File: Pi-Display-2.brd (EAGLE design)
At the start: 24.8 x 64.8 mm, 13 parts, among them IC1 MCP2515-I/SO, IC2 MCP2562-E/SN, J1 RJ45 CAN.Bus, Q1 16MHz, U1 TSR 2-2450

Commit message: Layouts angepasst
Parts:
- added C7: 10µF/25V, rcl:C1206
- C6: value 22µF 50V Low-ESR -> 10µF/25V; device rcl:E2-5 -> rcl:C1206
- moved C6 2.17 mm to (21.0, 58.1), flipped to the bottom, turned to 270 degrees
- moved C2 1.62 mm to (22.2, 31.8)
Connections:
- net +24V: now also C6.1, C7.1; no longer C6.+
- net GND: now also C6.2, C7.2; no longer C6.-
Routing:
- net GND: track 9.68 -> 12.4 mm
- net +5V: track 95.2 -> 96.9 mm
- net SPI_MOSI: track 7.75 -> 9.02 mm
- net +24V: track 64.4 -> 65.0 mm

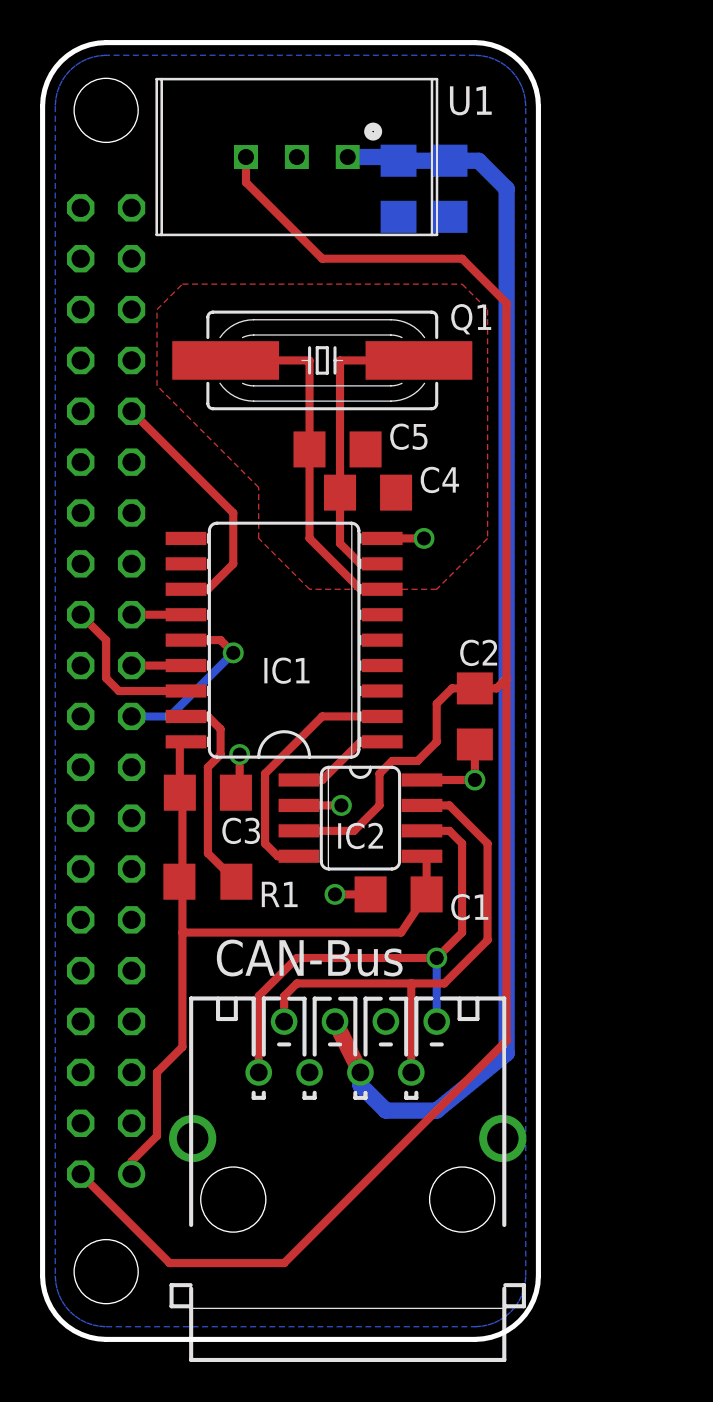
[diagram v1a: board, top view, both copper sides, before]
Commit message: CAN-Bus Beadboard-Adapter, Layouts angepasst
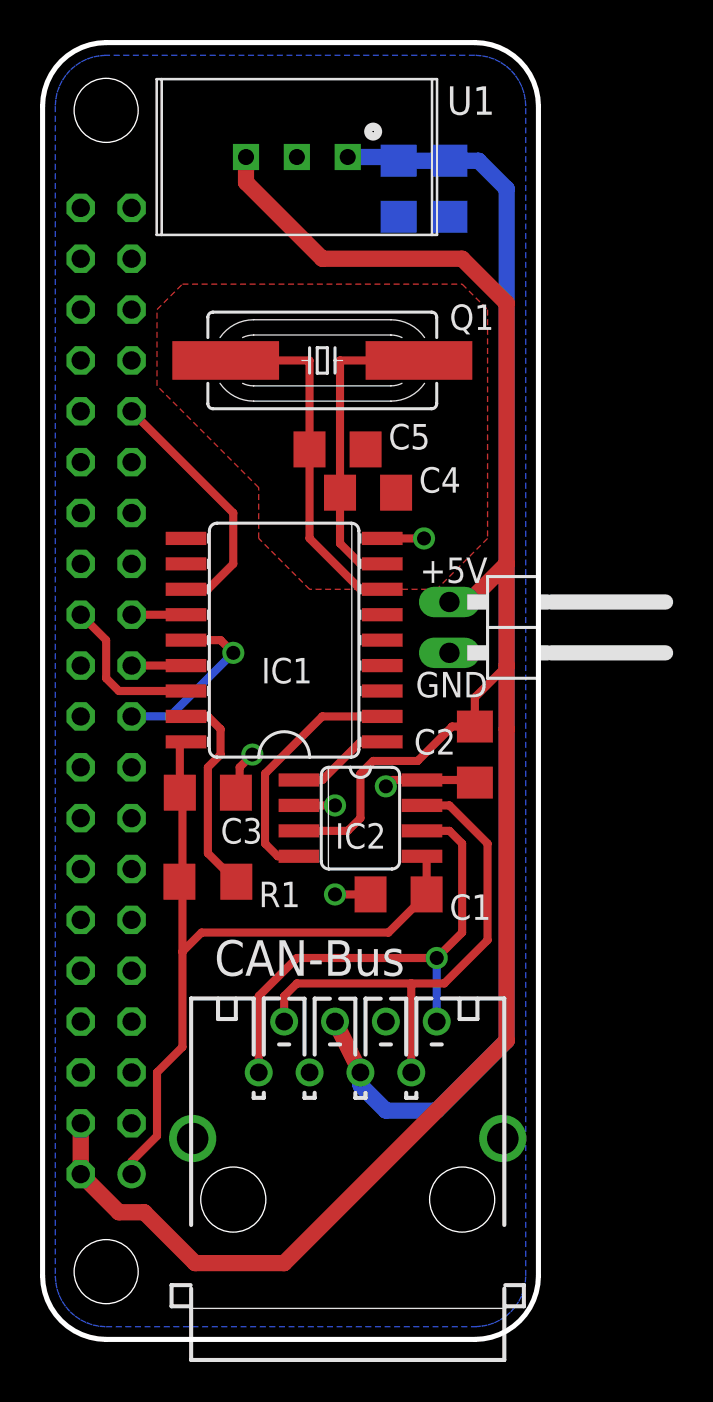
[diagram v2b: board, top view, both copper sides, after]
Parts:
- added JP1: Power-Display, pinhead:1X02/90
- moved C2 1.91 mm to (22.2, 29.8)
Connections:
- net +5V: now also JP1.1, SV1.4
- net GND: now also JP1.2
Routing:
- net +5V: track 96.9 -> 103.7 mm
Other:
- board text added: "+5V"
- board text added: "GND"

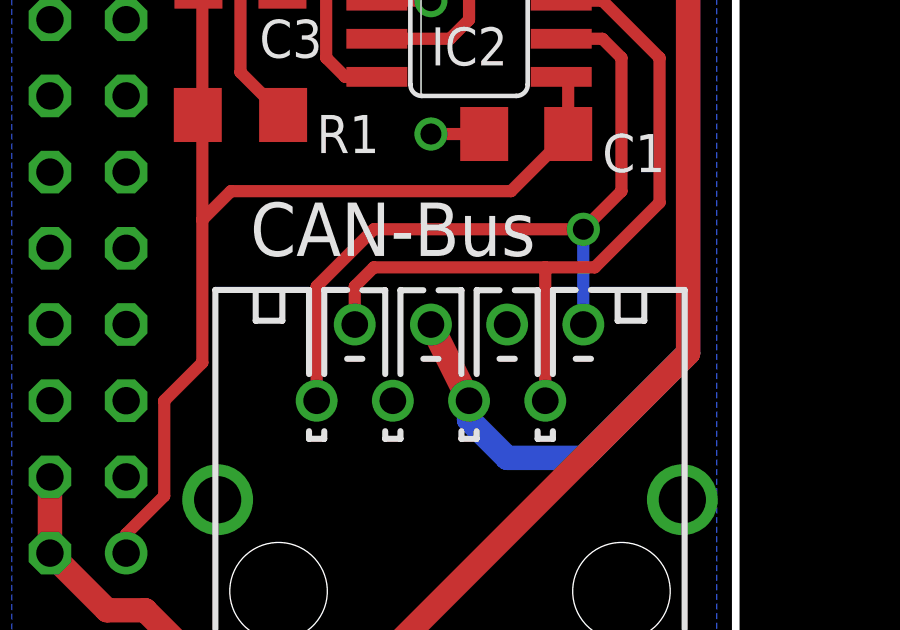
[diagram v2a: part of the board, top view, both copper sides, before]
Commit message: Layouts angepasst, Backplane vergrößert
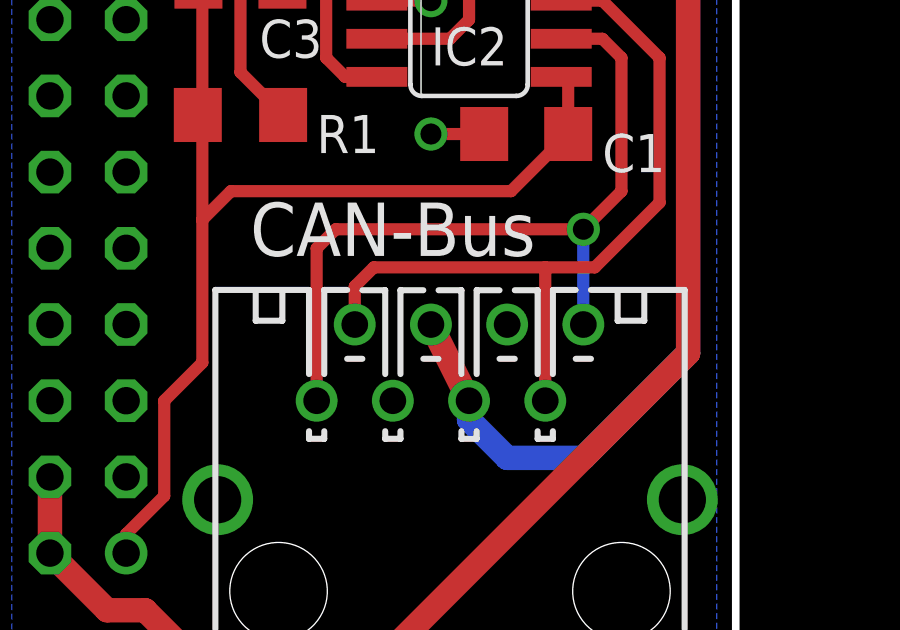
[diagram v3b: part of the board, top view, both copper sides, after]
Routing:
- net CANL: track 25.2 -> 25.9 mm
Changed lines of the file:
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@@
 <contactref element="J1" pad="1"/>
 <contactref element="J1" pad="8"/>
-<wire x1="13.335" y1="19.685" x2="11.43" y2="17.78" width="0.4064" layer="1"/>
-<wire x1="11.43" y1="17.78" x2="11.43" y2="13.97" width="0.4064" layer="1"/>
+<wire x1="12.065" y1="19.685" x2="11.43" y2="19.05" width="0.4064" layer="1"/>
+<wire x1="11.43" y1="19.05" x2="11.43" y2="13.97" width="0.4064" layer="1"/>
 <wire x1="20.32" y1="16.51" x2="20.32" y2="19.685" width="0.4064" layer="16"/>
 <via x="20.32" y="19.685" extent="1-16" drill="0.7"/>
-<wire x1="20.32" y1="19.685" x2="13.335" y2="19.685" width="0.4064" layer="1"/>
+<wire x1="12.065" y1="19.685" x2="20.32" y2="19.685" width="0.4064" layer="1"/>
 <wire x1="19.5834" y1="26.035" x2="20.955" y2="26.035" width="0.4064" layer="1"/>
 <wire x1="20.955" y1="26.035" x2="21.59" y2="25.4" width="0.4064" layer="1"/>
